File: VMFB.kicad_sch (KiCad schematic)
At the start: 109 parts, among them J1 Barrel_Jack_Switch, J10 Conn_01x03_Pin, J11 Conn_01x06_Pin, J12 Conn_01x04_Pin, J13 Conn_01x04_Pin, J14 Conn_01x04_Pin, J2 USB_B, J3 Screw_Terminal_01x02, J4 Screw_Terminal_01x03, J5 Conn_01x03_Pin, J6 Conn_01x04_Pin, J7 Conn_01x04_Pin, J8 Conn_01x04_Pin, J9 Conn_01x02_Pin, Q1 BC547, Q2 BC547, Q3 BC547, Q4 BD139, Q5 TIP41C, Q6 BC547, U1 LM358, U2 NE555P, U3 NE555P, U4 NE555P, U5 NE555P

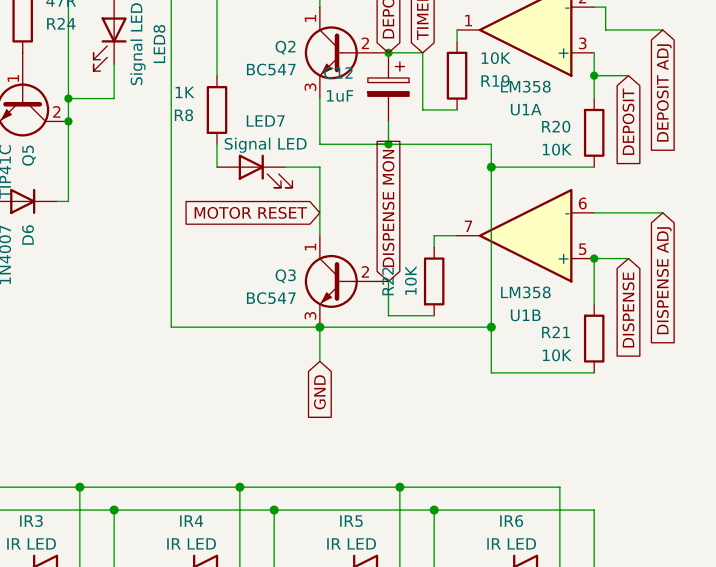
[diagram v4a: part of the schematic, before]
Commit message: added another 1uf cap across the dispense sensor so like the dispense sensor it won't trigger on power up.
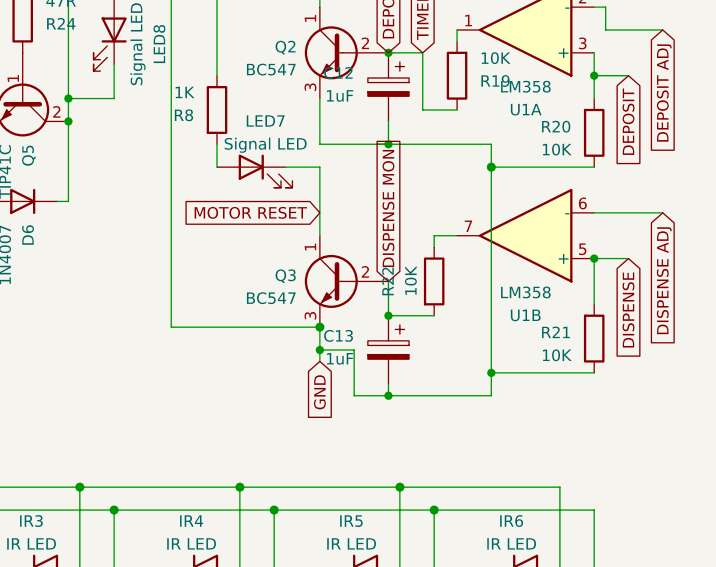
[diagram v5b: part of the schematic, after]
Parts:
- added C13: 1uF, Capacitor_THT:CP_Radial_D5.0mm_P2.00mm, symbol Device:C_Polarized
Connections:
- net DISPENSE MON: now also C13.1
- net GND: now also C13.2
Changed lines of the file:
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@@
   (junction (at 252.73 102.87) (diameter 1) (color 153 12 207 1)
   )
+  (junction (at 251.46 92.71) (diameter 0) (color 0 0 0 0)
+  )
   (junction (at 57.15 130.81) (diameter 0) (color 0 0 0 1)
   )
@@
   (junction (at 97.79 127) (diameter 1) (color 0 0 0 1)
   )
+  (junction (at 243.84 87.63) (diameter 0) (color 0 0 0 0)
+  )
   (junction (at 152.4 27.94) (diameter 0) (color 194 0 0 1)
   )
@@
   (junction (at 274.32 41.91) (diameter 0) (color 0 0 0 0)
   )
-  (junction (at 262.89 85.09) (diameter 1) (color 0 0 0 1)
-  )
   (junction (at 242.57 128.27) (diameter 0) (color 0 0 0 1)
   )
@@
   (junction (at 127 71.12) (diameter 1) (color 0 0 0 1)
   )
+  (junction (at 251.46 83.82) (diameter 0) (color 0 0 0 0)
+  )
   (junction (at 72.39 115.57) (diameter 0) (color 0 0 0 0)
   )
+  (junction (at 262.89 90.17) (diameter 0) (color 0 0 0 0)
+  )
   (junction (at 17.78 58.42) (diameter 0) (color 0 0 0 1)
   )
@@
     (stroke (width 0) (type default))
   )
+  (wire (pts (xy 251.46 92.71) (xy 262.89 92.71))
+    (stroke (width 0) (type default) (color 0 0 0 1))
+  )
   (wire (pts (xy 46.99 180.34) (xy 46.99 184.15))
     (stroke (width 0) (type default) (color 0 0 0 1))
@@
     (stroke (width 0) (type default) (color 0 0 0 1))
   )
+  (wire (pts (xy 251.46 91.44) (xy 251.46 92.71))
+    (stroke (width 0) (type default))
+  )
   (wire (pts (xy 72.39 109.22) (xy 72.39 115.57))
     (stroke (width 0) (type default))
@@
     (stroke (width 0) (type default) (color 153 12 207 1))
   )
-  (wire (pts (xy 262.89 90.17) (xy 262.89 85.09))
+  (wire (pts (xy 262.89 67.31) (xy 262.89 90.17))
     (stroke (width 0) (type default) (color 0 0 0 1))
   )
@@
     (stroke (width 0) (type default) (color 194 0 0 1))
   )
+  (wire (pts (xy 262.89 92.71) (xy 262.89 90.17))
+    (stroke (width 0) (type default) (color 0 0 0 1))
+  )
   (wire (pts (xy 20.32 48.26) (xy 33.02 48.26))
     (stroke (width 0) (type default) (color 255 221 0 1))
@@
     (stroke (width 0) (type default) (color 255 221 0 1))
   )
-  (wire (pts (xy 243.84 85.09) (xy 262.89 85.09))
+  (wire (pts (xy 247.65 92.71) (xy 251.46 92.71))
     (stroke (width 0) (type default) (color 0 0 0 1))
   )
@@
     (stroke (width 0) (type default) (color 0 255 0 1))
   )
+  (wire (pts (xy 247.65 87.63) (xy 243.84 87.63))
+    (stroke (width 0) (type default) (color 0 0 0 1))
+  )
   (wire (pts (xy 201.93 160.02) (xy 220.98 160.02))
     (stroke (width 0) (type default) (color 255 0 0 1))
@@
     (stroke (width 0) (type default))
   )
+  (wire (pts (xy 243.84 87.63) (xy 243.84 88.9))
+    (stroke (width 0) (type default) (color 0 0 0 1))
+  )
   (wire (pts (xy 200.66 46.99) (xy 200.66 49.53))
     (stroke (width 0) (type default))
@@
     (stroke (width 0) (type default))
   )
-  (wire (pts (xy 243.84 85.09) (xy 243.84 88.9))
-    (stroke (width 0) (type default) (color 0 0 0 1))
-  )
   (wire (pts (xy 220.98 22.86) (xy 207.01 22.86))
     (stroke (width 0) (type default) (color 194 0 0 1))
@@
     (stroke (width 0) (type default))
   )
+  (wire (pts (xy 243.84 87.63) (xy 243.84 85.09))
+    (stroke (width 0) (type default) (color 0 0 0 1))
+  )
   (wire (pts (xy 224.79 162.56) (xy 224.79 154.94))
     (stroke (width 0) (type default) (color 0 0 0 1))
@@
     (stroke (width 0) (type default))
   )
-  (wire (pts (xy 262.89 67.31) (xy 262.89 85.09))
-    (stroke (width 0) (type default) (color 0 0 0 1))
-  )
   (wire (pts (xy 208.28 54.61) (xy 208.28 44.45))
     (stroke (width 0) (type default) (color 194 0 0 1))
@@
     (stroke (width 0) (type default))
   )
+  (wire (pts (xy 247.65 92.71) (xy 247.65 87.63))
+    (stroke (width 0) (type default) (color 0 0 0 1))
+  )
   (wire (pts (xy 255.27 160.02) (xy 260.35 160.02))
     (stroke (width 0) (type default) (color 255 153 0 1))
@@
         )
       )
+    )
+  )
+  (symbol (lib_id "Device:C_Polarized") (at 251.46 87.63 0) (mirror y) (unit 1)
+    (in_bom yes) (on_board yes) (dnp no)
+    (property "Reference" "C13" (at 247.65 86.106 0)
+      (effects (font (size 1.27 1.27)) (justify left))
+    )
+    (property "Value" "1uF" (at 247.65 88.646 0)
+      (effects (font (size 1.27 1.27)) (justify left))
+    )
+    (property "Footprint" "Capacitor_THT:CP_Radial_D5.0mm_P2.00mm" (at 250.4948 91.44 0)
+      (effects (font (size 1.27 1.27)) hide)
+    )
+    (property "Datasheet" "~" (at 251.46 87.63 0)
+      (effects (font (size 1.27 1.27)) hide)
+    )
+    (pin "1")
+    (pin "2")
+    (instances
+      (project "VMFB"
+        (path "/840789ee-60d4-4003-8113-c1b030a45492"
+          (reference "C13") (unit 1)
+        )
+      )

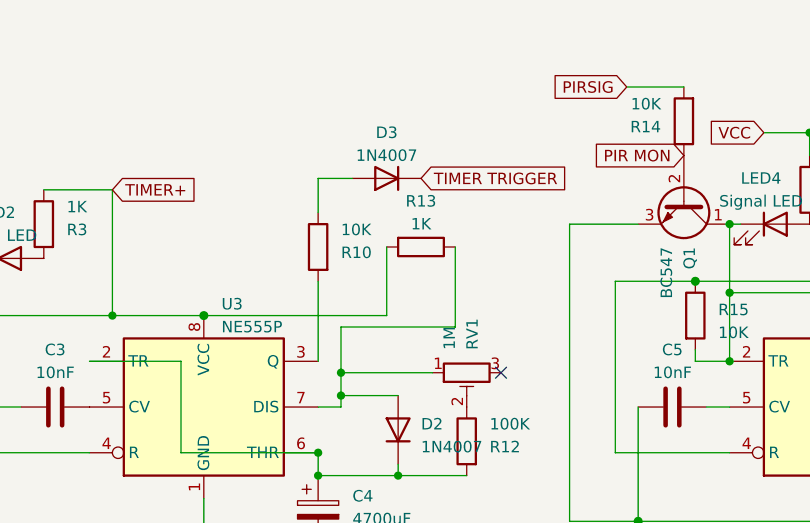
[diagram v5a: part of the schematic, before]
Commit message: added resistor and diode to turn IR LEDs on when the timer triggers so the dispense sensors can stop the motor
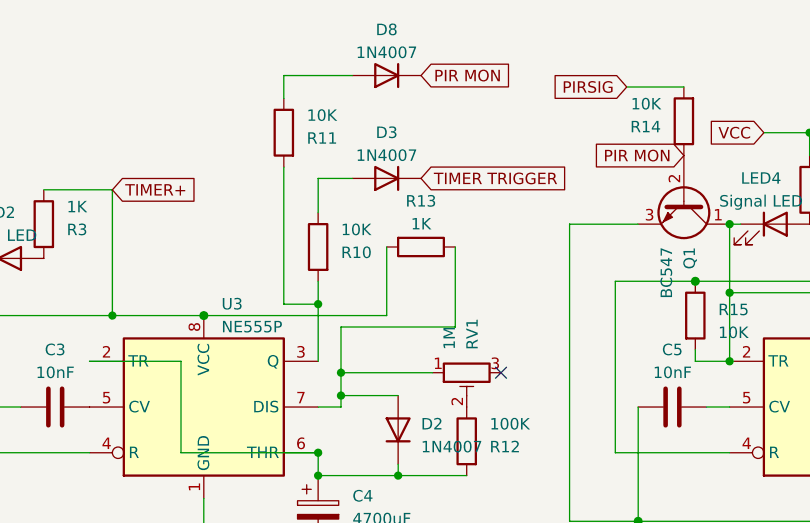
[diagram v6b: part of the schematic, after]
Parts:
- added D8: 1N4007, Diode_THT:D_DO-41_SOD81_P2.54mm_Vertical_KathodeUp, symbol Diode:1N4007
- added R11: 10K, Resistor_THT:R_Axial_DIN0207_L6.3mm_D2.5mm_P2.54mm_Vertical, symbol Device:R
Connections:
- net PIR MON: now also D8.1 (K)
- net at R10.2, U3.3 (Q): now also R11.2
- new net: D8.2 (A), R11.1
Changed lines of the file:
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@@
   (junction (at 114.3 44.45) (diameter 1) (color 194 0 0 1)
   )
+  (junction (at 55.88 46.99) (diameter 0) (color 0 0 0 0)
+  )
   (junction (at 101.6 45.72) (diameter 0) (color 0 0 0 0)
   )
@@
     (stroke (width 0) (type default))
   )
+  (wire (pts (xy 52.07 21.59) (xy 59.69 21.59))
+    (stroke (width 0) (type default))
+  )
   (wire (pts (xy 274.32 90.17) (xy 262.89 90.17))
     (stroke (width 0) (type default) (color 0 0 0 1))
@@
     (stroke (width 0) (type solid) (color 255 255 0 1))
   )
-  (wire (pts (xy 55.88 44.45) (xy 55.88 53.34))
+  (wire (pts (xy 55.88 44.45) (xy 55.88 46.99))
     (stroke (width 0) (type default))
   )
@@
     (stroke (width 0) (type default))
   )
+  (wire (pts (xy 52.07 31.75) (xy 52.07 46.99))
+    (stroke (width 0) (type default))
+  )
   (wire (pts (xy 210.82 46.99) (xy 200.66 46.99))
     (stroke (width 0) (type default))
@@
     (stroke (width 0) (type default) (color 194 0 0 1))
   )
+  (wire (pts (xy 52.07 46.99) (xy 55.88 46.99))
+    (stroke (width 0) (type default))
+  )
   (wire (pts (xy 256.54 125.73) (xy 274.32 125.73))
     (stroke (width 0) (type default) (color 0 255 0 1))
@@
     (stroke (width 0) (type default))
   )
+  (wire (pts (xy 52.07 24.13) (xy 52.07 21.59))
+    (stroke (width 0) (type default))
+  )
   (wire (pts (xy 217.17 102.87) (xy 217.17 111.76))
     (stroke (width 0) (type default) (color 153 12 207 1))
@@
     (stroke (width 0) (type default))
   )
+  (wire (pts (xy 55.88 46.99) (xy 55.88 53.34))
+    (stroke (width 0) (type default))
+  )
   (wire (pts (xy 187.96 64.77) (xy 187.96 71.12))
     (stroke (width 0) (type default) (color 0 0 0 1))
@@
     )
   )
+  (global_label "PIR MON" (shape input) (at 67.31 21.59 0) (fields_autoplaced)
+    (effects (font (size 1.27 1.27)) (justify left))
+    (property "Intersheetrefs" "${INTERSHEET_REFS}" (at 78.4406 21.59 0) (show_name)
+      (effects (font (size 1.27 1.27)) (justify left) hide)
+    )
+  )
   (global_label "GND" (shape input) (at 170.18 118.11 90) (fields_autoplaced)
     (effects (font (size 1.27 1.27)) (justify left))
@@
     )
   )
+  (symbol (lib_id "Diode:1N4007") (at 63.5 21.59 180) (unit 1)
+    (in_bom yes) (on_board yes) (dnp no)
+    (property "Reference" "D8" (at 63.5 16.51 0)
+      (effects (font (size 1.27 1.27)))
+    )
+    (property "Value" "1N4007" (at 63.5 19.05 0)
+      (effects (font (size 1.27 1.27)))
+    )
+    (property "Footprint" "Diode_THT:D_DO-41_SOD81_P2.54mm_Vertical_KathodeUp" (at 63.5 17.145 0)
+      (effects (font (size 1.27 1.27)) hide)
+    )
+    (property "Datasheet" "http://www.vishay.com/docs/88503/1n4001.pdf" (at 63.5 21.59 0)
+      (effects (font (size 1.27 1.27)) hide)
+    )
+    (property "Sim.Device" "D" (at 63.5 21.59 0)
+      (effects (font (size 1.27 1.27)) hide)
+    )
+    (property "Sim.Pins" "1=K 2=A" (at 63.5 21.59 0)
+      (effects (font (size 1.27 1.27)) hide)
+    )
+    (pin "1")
+    (pin "2")
+    (instances
+      (project "VMFB"
+        (path "/840789ee-60d4-4003-8113-c1b030a45492"
+          (reference "D8") (unit 1)
+        )
+      )
+    )
+  )
   (symbol (lib_id "Device:R") (at 72.39 105.41 0) (mirror y) (unit 1)
     (in_bom yes) (on_board yes) (dnp no)
@@
         )
       )
+    )
+  )
+  (symbol (lib_id "Device:R") (at 52.07 27.94 0) (mirror y) (unit 1)
+    (in_bom yes) (on_board yes) (dnp no)
+    (property "Reference" "R11" (at 54.61 28.575 0)
+      (effects (font (size 1.27 1.27)) (justify right))
+    )
+    (property "Value" "10K" (at 54.61 26.035 0)
+      (effects (font (size 1.27 1.27)) (justify right))
+    )
+    (property "Footprint" "Resistor_THT:R_Axial_DIN0207_L6.3mm_D2.5mm_P2.54mm_Vertical" (at 53.848 27.94 90)
+      (effects (font (size 1.27 1.27)) hide)
+    )
+    (property "Datasheet" "~" (at 52.07 27.94 0)
+      (effects (font (size 1.27 1.27)) hide)
+    )
+    (pin "1")
+    (pin "2")
+    (instances
+      (project "VMFB"
+        (path "/840789ee-60d4-4003-8113-c1b030a45492"
+          (reference "R11") (unit 1)
+        )
+      )

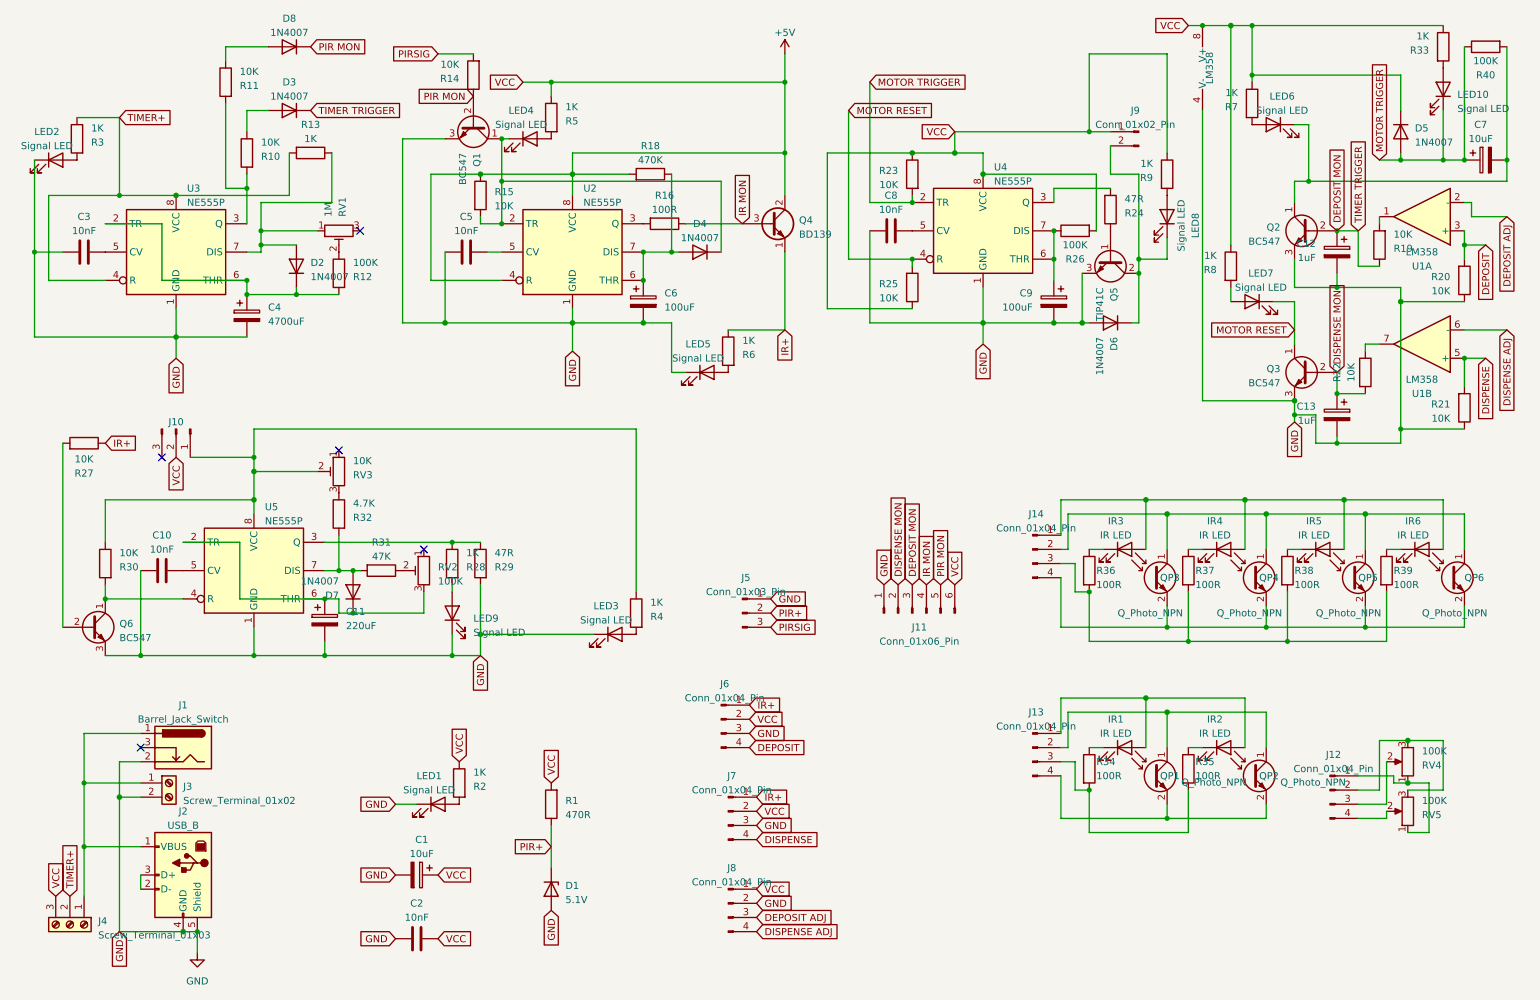
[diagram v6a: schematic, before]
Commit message: a few small tweaks, connecting the switch pin of the barrel jack to ground
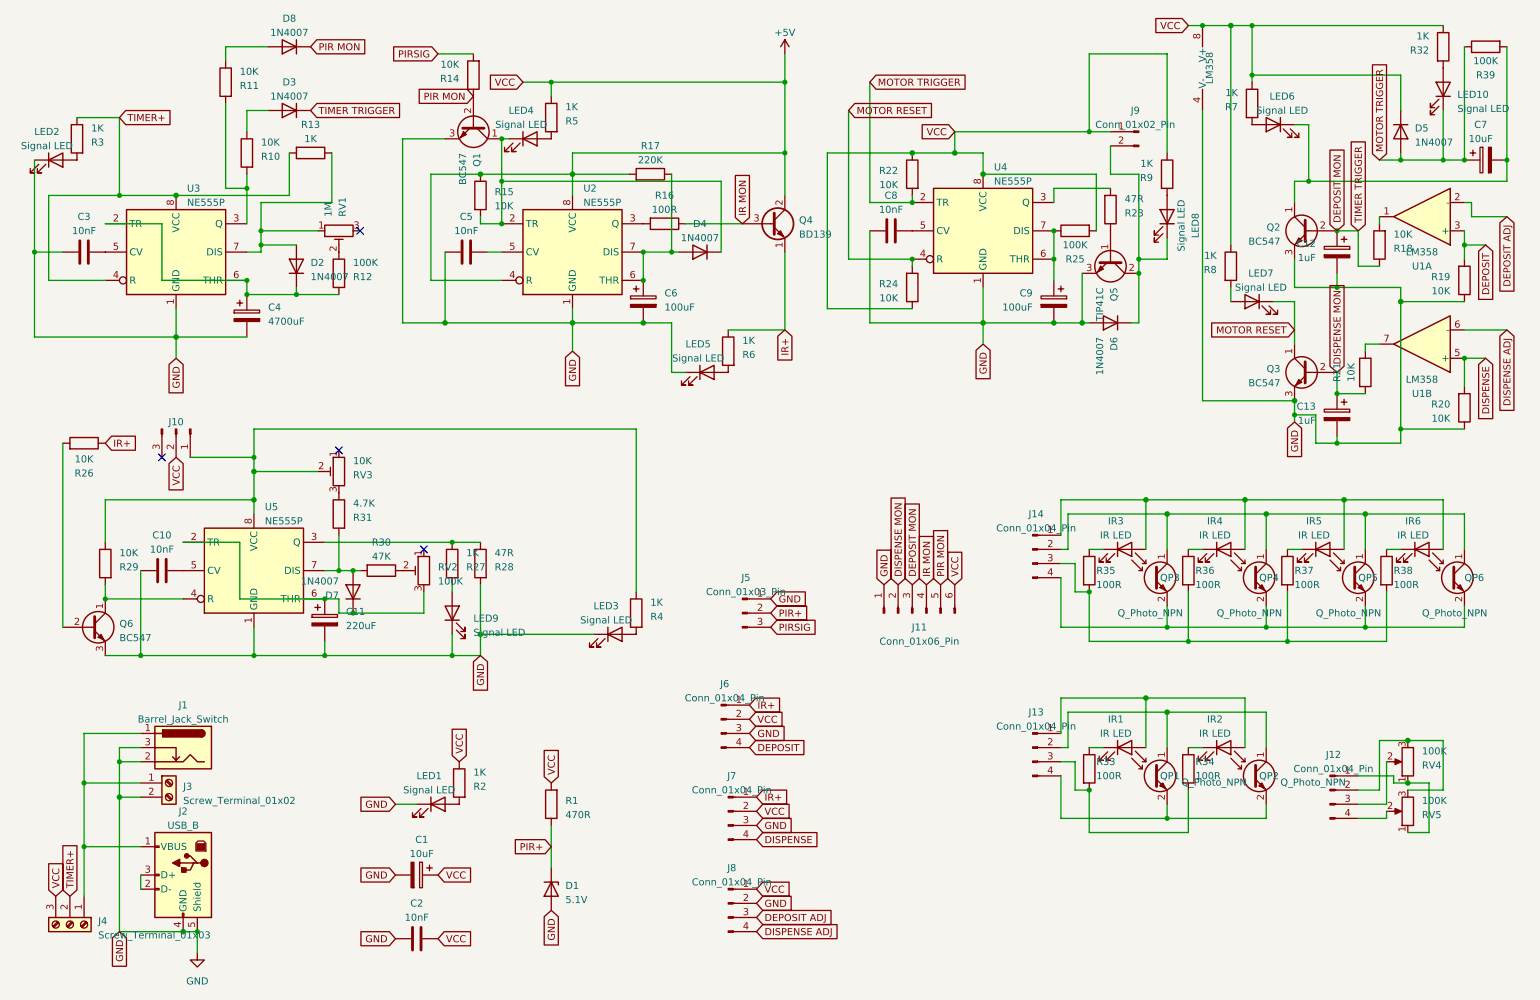
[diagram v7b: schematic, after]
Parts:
- R17: renamed from R18; value 470K -> 220K
- renumbered R19 to R18, R20 to R19, R21 to R20, R22 to R21, R23 to R22, R24 to R23, R25 to R24, R26 to R25, R27 to R26, R28 to R27, R29 to R28, R30 to R29, R31 to R30, R32 to R31, R33 to R32, R34 to R33, R35 to R34, R36 to R35, R37 to R36, R38 to R37, R39 to R38, R40 to R39
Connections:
- net GND: now also J1.3
- no-connect marks 5 -> 4
